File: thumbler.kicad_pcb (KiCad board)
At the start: 2 copper layers, 128 parts, among them J1 Conn_01x07, J2 Conn_01x05, J3 Conn_01x07, J4 Conn_01x05

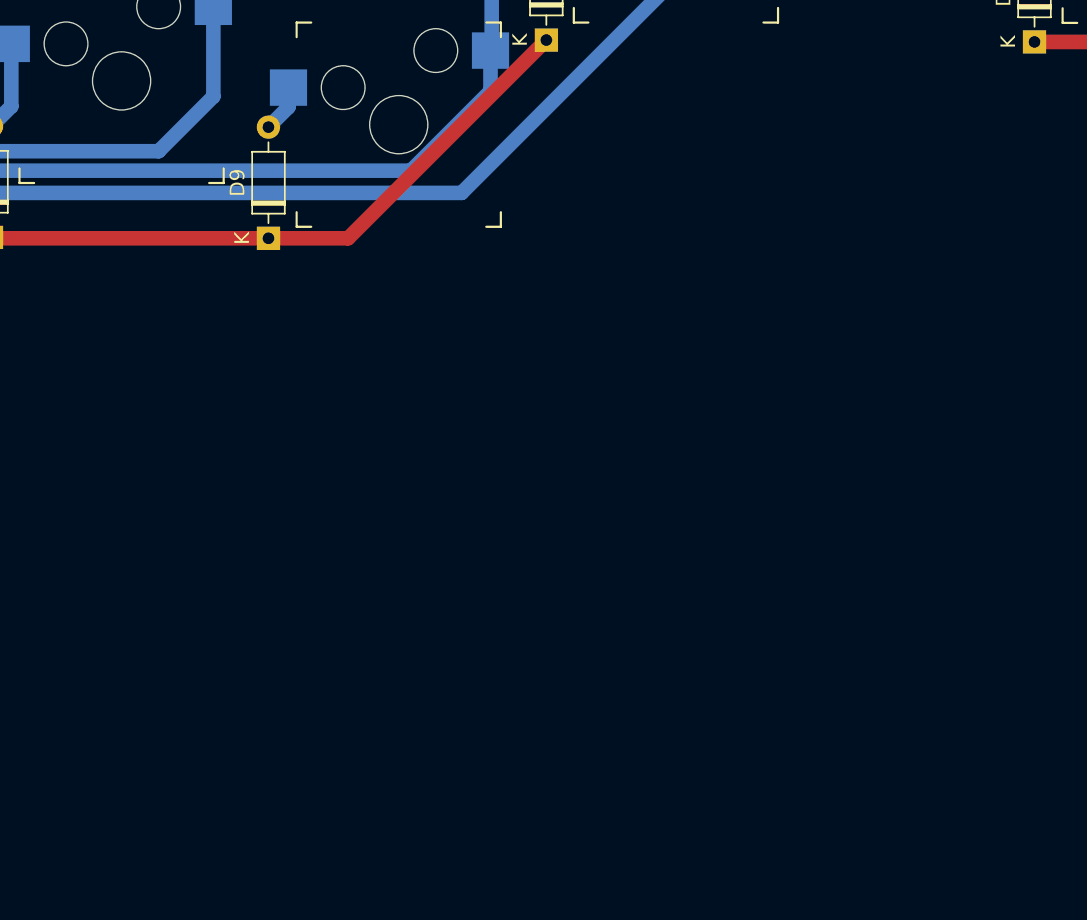
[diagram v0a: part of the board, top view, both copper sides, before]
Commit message: add footprint for ANO
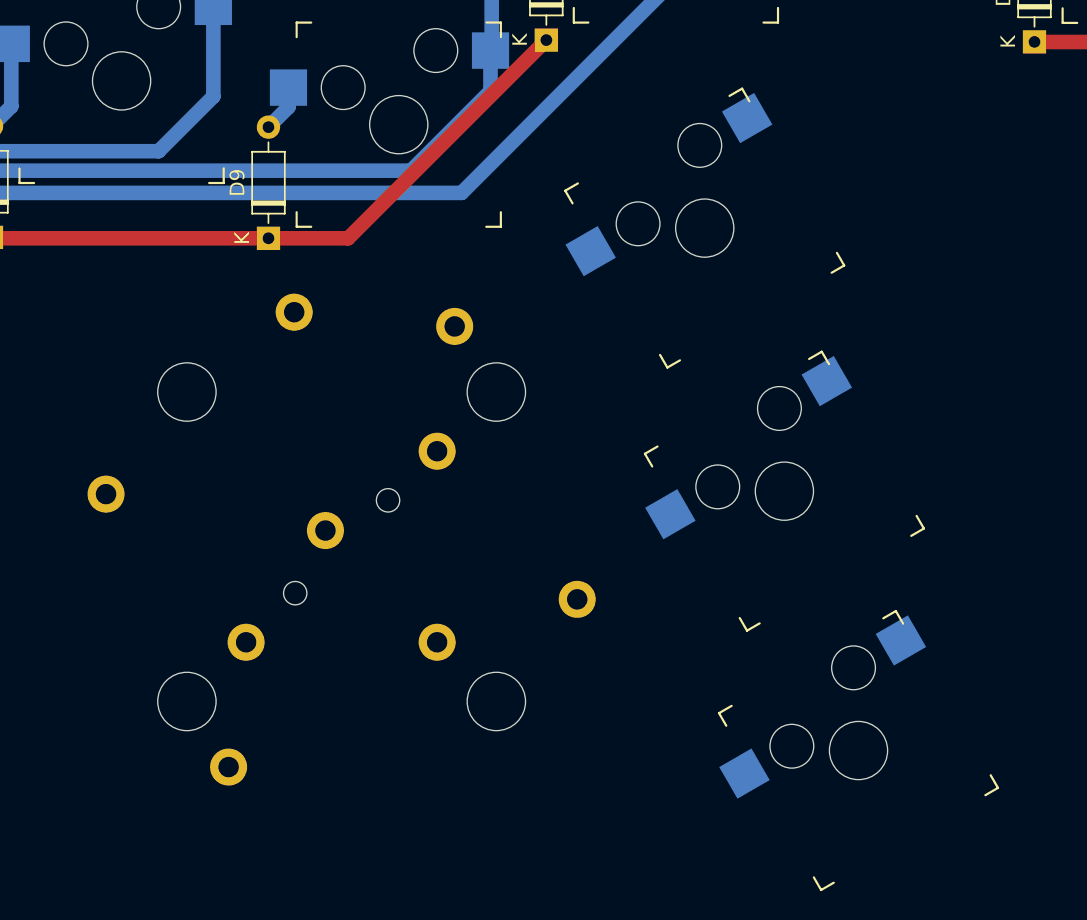
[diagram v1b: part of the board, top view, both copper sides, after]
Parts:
- added S9: Kailh_Hotplug, keyswitches:Kailh_socket_MX_platemount, F.Cu at (290.6, 222.8)
- added S9: Kailh_Hotplug, keyswitches:Kailh_socket_MX_platemount, F.Cu at (285.5, 205.0)
- added S9: Kailh_Hotplug, keyswitches:Kailh_socket_MX_platemount, F.Cu at (280.0, 187.0)
- added X1: ENCODER_ANO, ENCODER_ANO, B.Cu at (255.1, 208.8)

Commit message: more protection, more footprints
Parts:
- removed J3: Conn_01x07, Connector_PinHeader_2.54mm:PinHeader_1x07_P2.54mm_Vertical
- removed the S9 at (290.6, 222.8)
- removed the S9 at (285.5, 205.0)
- removed the S9 at (280.0, 187.0)
- added C1: 1u, Capacitor_SMD:C_0805_2012Metric_Pad1.18x1.45mm_HandSolder, F.Cu at (341.6, 301.8)
- added C10: 10n, Capacitor_SMD:C_0805_2012Metric_Pad1.18x1.45mm_HandSolder, F.Cu at (200.1, 314.3)
- added C11: Cext, Capacitor_SMD:C_0805_2012Metric_Pad1.18x1.45mm_HandSolder, F.Cu at (341.6, 298.8)
- added C12: Cext, Capacitor_SMD:C_0805_2012Metric_Pad1.18x1.45mm_HandSolder, F.Cu at (331.7, 307.5)
- added C13: 1u, Capacitor_SMD:C_0805_2012Metric_Pad1.18x1.45mm_HandSolder, F.Cu at (356.5, 282.2)
- added C14: 1u, Capacitor_SMD:C_0805_2012Metric_Pad1.18x1.45mm_HandSolder, F.Cu at (331.7, 310.5)
- added C15: 4u7, Capacitor_SMD:C_0805_2012Metric_Pad1.18x1.45mm_HandSolder, F.Cu at (214.4, 319.8)
- added C16: 4u7, Capacitor_SMD:C_0805_2012Metric_Pad1.18x1.45mm_HandSolder, F.Cu at (318.5, 321.0)
- added C17: 100n, Capacitor_SMD:C_0805_2012Metric_Pad1.18x1.45mm_HandSolder, F.Cu at (312.5, 328.2)
- added C18: 100n, Capacitor_SMD:C_0805_2012Metric_Pad1.18x1.45mm_HandSolder, F.Cu at (304.1, 339.5)
- added C19: 100n, Capacitor_SMD:C_0805_2012Metric_Pad1.18x1.45mm_HandSolder, F.Cu at (361.3, 282.2)
- added C2: 1u, Capacitor_SMD:C_0805_2012Metric_Pad1.18x1.45mm_HandSolder, F.Cu at (204.9, 314.3)
- added C20: 1u, Capacitor_SMD:C_0805_2012Metric_Pad1.18x1.45mm_HandSolder, F.Cu at (336.2, 304.1)
- added C21: 10n, Capacitor_SMD:C_0805_2012Metric_Pad1.18x1.45mm_HandSolder, F.Cu at (306.5, 335.3)
- added C22: 100n, Capacitor_SMD:C_0805_2012Metric_Pad1.18x1.45mm_HandSolder, F.Cu at (356.5, 285.2)
- added C3: 4u7, Capacitor_SMD:C_0805_2012Metric_Pad1.18x1.45mm_HandSolder, F.Cu at (209.7, 314.3)
- added C4: 4u7, Capacitor_SMD:C_0805_2012Metric_Pad1.18x1.45mm_HandSolder, F.Cu at (214.5, 314.3)
- added C5: 100n, Capacitor_SMD:C_0805_2012Metric_Pad1.18x1.45mm_HandSolder, F.Cu at (214.2, 330.7)
- added C6: 100n, Capacitor_SMD:C_0805_2012Metric_Pad1.18x1.45mm_HandSolder, F.Cu at (214.5, 325.3)
- added C7: 100n, Capacitor_SMD:C_0805_2012Metric_Pad1.18x1.45mm_HandSolder, F.Cu at (306.5, 332.3)
- added C8: 1u, Capacitor_SMD:C_0805_2012Metric_Pad1.18x1.45mm_HandSolder, F.Cu at (324.5, 316.9)
- added C9: 100n, Capacitor_SMD:C_0805_2012Metric_Pad1.18x1.45mm_HandSolder, F.Cu at (349.3, 290.3)
- added D63: RED, LED_SMD:LED_1206_3216Metric_Pad1.42x1.75mm_HandSolder, F.Cu at (190.1, 81.6)
- added D64: 1N4148, Diode_THT:D_DO-35_SOD27_P7.62mm_Horizontal, F.Cu at (272.2, 199.0)
- added D65: 1N4148, Diode_THT:D_DO-35_SOD27_P7.62mm_Horizontal, F.Cu at (270.6, 220.5)
- added D66: 1N4148, Diode_THT:D_DO-35_SOD27_P7.62mm_Horizontal, F.Cu at (269.4, 240.7)
- added D67: RED, LED_SMD:LED_1206_3216Metric_Pad1.42x1.75mm_HandSolder, F.Cu at (307.1, 329.1)
- added D68: WHITE, LED_SMD:LED_1206_3216Metric_Pad1.42x1.75mm_HandSolder, F.Cu at (467.2, 77.7)
- added D69: 1N4148, Diode_THT:D_DO-35_SOD27_P7.62mm_Horizontal, F.Cu at (343.2, 198.0)
- added D70: 1N4148, Diode_THT:D_DO-35_SOD27_P7.62mm_Horizontal, F.Cu at (347.3, 217.8)
- added D71: 1N4148, Diode_THT:D_DO-35_SOD27_P7.62mm_Horizontal, F.Cu at (353.1, 236.5)
- added D72: WHITE, LED_SMD:LED_1206_3216Metric_Pad1.42x1.75mm_HandSolder, F.Cu at (467.2, 82.5)
- added D73: WHITE, LED_SMD:LED_1206_3216Metric_Pad1.42x1.75mm_HandSolder, F.Cu at (467.2, 72.9)
- added D74: B5819W, Diode_SMD:D_SOD-123, F.Cu at (196.7, 63.8)
- added D75: B5819W, Diode_SMD:D_SOD-123, F.Cu at (409.4, 62.6)
- added F1: 350mA, Resistor_SMD:R_1812_4532Metric_Pad1.30x3.40mm_HandSolder, F.Cu at (184.7, 63.7)
- added F2: 350mA, Resistor_SMD:R_1812_4532Metric_Pad1.30x3.40mm_HandSolder, F.Cu at (399.4, 62.4)
- added FB1: 90R @ 100MHz, Inductor_SMD:L_0805_2012Metric_Pad1.15x1.40mm_HandSolder, F.Cu at (318.5, 324.0)
- added FB2: 90R @ 100MHz, Inductor_SMD:L_0805_2012Metric_Pad1.15x1.40mm_HandSolder, F.Cu at (420.3, 62.7)
- added J6: Conn_01x04, Connector_PinHeader_2.54mm:PinHeader_2x02_P2.54mm_Vertical, F.Cu at (149.4, 199.6)
- added J7: DIN-5_180degree, Connector_DIN:DIN5_180_CP-2350, F.Cu at (362.9, 79.9)
- added J8: Conn_01x04, Connector_PinHeader_2.54mm:PinHeader_2x02_P2.54mm_Vertical, F.Cu at (497.6, 194.4)
- added JP1: SolderJumper_2_Open, Jumper:SolderJumper-2_P1.3mm_Open_TrianglePad1.0x1.5mm, F.Cu at (261.3, 68.0)
- added R1: 470R, Resistor_SMD:R_0805_2012Metric_Pad1.20x1.40mm_HandSolder, F.Cu at (323.3, 321.0)
- added R10: 470R, Resistor_SMD:R_0805_2012Metric_Pad1.20x1.40mm_HandSolder, F.Cu at (323.3, 323.9)
- added R11: 470R, Resistor_SMD:R_0805_2012Metric_Pad1.20x1.40mm_HandSolder, F.Cu at (316.1, 331.2)
- added R12: 470R, Resistor_SMD:R_0805_2012Metric_Pad1.20x1.40mm_HandSolder, F.Cu at (328.0, 319.9)
- added R13: 470R, Resistor_SMD:R_0805_2012Metric_Pad1.20x1.40mm_HandSolder, F.Cu at (346.3, 302.1)
- added R14: 470R, Resistor_SMD:R_0805_2012Metric_Pad1.20x1.40mm_HandSolder, F.Cu at (352.4, 296.2)
- added R15: 470R, Resistor_SMD:R_0805_2012Metric_Pad1.20x1.40mm_HandSolder, F.Cu at (334.0, 316.4)
- added R16: 10K, Resistor_SMD:R_0805_2012Metric_Pad1.20x1.40mm_HandSolder, F.Cu at (328.0, 322.8)
- added R17: 470R, Resistor_SMD:R_0805_2012Metric_Pad1.20x1.40mm_HandSolder, F.Cu at (316.1, 334.1)
- added R18: 470R, Resistor_SMD:R_0805_2012Metric_Pad1.20x1.40mm_HandSolder, F.Cu at (323.2, 326.9)
- added R19: 470R, Resistor_SMD:R_0805_2012Metric_Pad1.20x1.40mm_HandSolder, F.Cu at (347.7, 293.2)
- added R2: 10K, Resistor_SMD:R_0805_2012Metric_Pad1.20x1.40mm_HandSolder, F.Cu at (347.7, 296.2)
- added R20: 1K, Resistor_SMD:R_0805_2012Metric_Pad1.20x1.40mm_HandSolder, F.Cu at (341.2, 307.7)
- added R21: 1K, Resistor_SMD:R_0805_2012Metric_Pad1.20x1.40mm_HandSolder, F.Cu at (336.5, 310.0)
- added R22: 470R, Resistor_SMD:R_0805_2012Metric_Pad1.20x1.40mm_HandSolder, F.Cu at (331.7, 313.4)
- added R23: 1K, Resistor_SMD:R_0805_2012Metric_Pad1.20x1.40mm_HandSolder, F.Cu at (355.3, 288.2)
- added R24: 470R, Resistor_SMD:R_0805_2012Metric_Pad1.20x1.40mm_HandSolder, B.Cu at (438.8, 184.6)
- added R25: 10K, Resistor_SMD:R_0805_2012Metric_Pad1.20x1.40mm_HandSolder, F.Cu at (352.4, 293.2)
- added R26: 470R, Resistor_SMD:R_0805_2012Metric_Pad1.20x1.40mm_HandSolder, F.Cu at (318.5, 326.9)
- added R27: 470R, Resistor_SMD:R_0805_2012Metric_Pad1.20x1.40mm_HandSolder, F.Cu at (329.3, 316.8)
- added R28: 470R, Resistor_SMD:R_0805_2012Metric_Pad1.20x1.40mm_HandSolder, F.Cu at (336.5, 307.1)
- added R3: 22R, Resistor_SMD:R_0805_2012Metric_Pad1.20x1.40mm_HandSolder, F.Cu at (346.3, 299.1)
- added R4: 1K, Resistor_SMD:R_0805_2012Metric_Pad1.20x1.40mm_HandSolder, F.Cu at (311.3, 335.2)
- added R5: 22R, Resistor_SMD:R_0805_2012Metric_Pad1.20x1.40mm_HandSolder, F.Cu at (172.7, 74.7)
- added R6: 22R, Resistor_SMD:R_0805_2012Metric_Pad1.20x1.40mm_HandSolder, F.Cu at (341.2, 304.8)
- added R7: 22R, Resistor_SMD:R_0805_2012Metric_Pad1.20x1.40mm_HandSolder, F.Cu at (361.3, 285.1)
- added R8: 1K, Resistor_SMD:R_0805_2012Metric_Pad1.20x1.40mm_HandSolder, F.Cu at (308.9, 338.2)
- added R9: 470R, Resistor_SMD:R_0805_2012Metric_Pad1.20x1.40mm_HandSolder, B.Cu at (189.3, 187.9)
- added S63: Kailh_Hotplug, keyswitches:Kailh_socket_MX_platemount, F.Cu at (281.2, 190.9)
- added S64: Kailh_Hotplug, keyswitches:Kailh_socket_MX_platemount, F.Cu at (279.5, 212.2)
- added S65: Kailh_Hotplug, keyswitches:Kailh_socket_MX_platemount, F.Cu at (278.3, 232.5)
- added S66: RKJXV122400R, Alps:RKJXV122400R, F.Cu at (382.8, 206.4)
- added S67: Kailh_Hotplug, keyswitches:Kailh_socket_MX_platemount, F.Cu at (352.2, 189.8)
- added S68: Kailh_Hotplug, keyswitches:Kailh_socket_MX_platemount, F.Cu at (356.2, 209.7)
- added S69: Kailh_Hotplug, keyswitches:Kailh_socket_MX_platemount, F.Cu at (361.9, 228.4)
- added SW1: SW_Push, Button_Switch_THT:SW_PUSH-12mm, B.Cu at (160.2, 199.2)
- added SW2: SW_DIP_x05, Button_Switch_THT:SW_DIP_SPSTx05_Slide_9.78x14.88mm_W7.62mm_P2.54mm, B.Cu at (161.2, 205.6)
- added SW3: SW_Push, Button_Switch_THT:SW_PUSH-12mm, B.Cu at (464.6, 200.1)
- added SW4: SW_DIP_x05, Button_Switch_THT:SW_DIP_SPSTx05_Slide_9.78x14.88mm_W7.62mm_P2.54mm, B.Cu at (465.8, 207.3)
- added TP1: TestPoint, TestPoint:TestPoint_Pad_D2.0mm, F.Cu at (161.5, 251.5)
- added TP10: TestPoint, TestPoint:TestPoint_Pad_D2.0mm, F.Cu at (155.9, 234.4)
- added TP11: TestPoint, TestPoint:TestPoint_Pad_D2.0mm, F.Cu at (149.8, 238.4)
- added TP12: TestPoint, TestPoint:TestPoint_Pad_D2.0mm, F.Cu at (149.0, 250.6)
- added TP13: TestPoint, TestPoint:TestPoint_Pad_D2.0mm, F.Cu at (145.8, 238.3)
- added TP14: TestPoint, TestPoint:TestPoint_Pad_D2.0mm, F.Cu at (158.4, 263.6)
- added TP15: TestPoint, TestPoint:TestPoint_Pad_D2.0mm, F.Cu at (153.1, 250.1)
- added TP16: TestPoint, TestPoint:TestPoint_Pad_D2.0mm, F.Cu at (159.1, 245.5)
- added TP17: TestPoint, TestPoint:TestPoint_Pad_D2.0mm, F.Cu at (165.6, 255.4)
- added TP18: TestPoint, TestPoint:TestPoint_Pad_D2.0mm, F.Cu at (153.9, 238.4)
- added TP19: TestPoint, TestPoint:TestPoint_Pad_D2.0mm, F.Cu at (148.7, 242.5)
- added TP2: TestPoint, TestPoint:TestPoint_Pad_D2.0mm, F.Cu at (155.0, 245.5)
- added TP20: TestPoint, TestPoint:TestPoint_Pad_D2.0mm, F.Cu at (169.6, 251.4)
- added TP21: TestPoint, TestPoint:TestPoint_Pad_D2.0mm, F.Cu at (422.8, 270.0)
- added TP22: TestPoint, TestPoint:TestPoint_Pad_D2.0mm, F.Cu at (422.6, 284.1)
- added TP23: TestPoint, TestPoint:TestPoint_Pad_D2.0mm, F.Cu at (429.0, 252.6)
- added TP24: TestPoint, TestPoint:TestPoint_Pad_D2.0mm, F.Cu at (422.8, 277.2)
- added TP25: TestPoint, TestPoint:TestPoint_Pad_D2.0mm, F.Cu at (433.1, 252.1)
- added TP26: TestPoint, TestPoint:TestPoint_Pad_D2.0mm, F.Cu at (421.2, 263.3)
- added TP27: TestPoint, TestPoint:TestPoint_Pad_D2.0mm, F.Cu at (419.5, 257.1)
- added TP28: TestPoint, TestPoint:TestPoint_Pad_D2.0mm, F.Cu at (428.9, 263.1)
- added TP29: TestPoint, TestPoint:TestPoint_Pad_D2.0mm, F.Cu at (430.9, 271.0)
- added TP3: TestPoint, TestPoint:TestPoint_Pad_D2.0mm, F.Cu at (151.9, 230.3)
- added TP30: TestPoint, TestPoint:TestPoint_Pad_D2.0mm, F.Cu at (429.2, 256.6)
- added TP31: TestPoint, TestPoint:TestPoint_Pad_D2.0mm, F.Cu at (431.7, 277.8)
- added TP32: TestPoint, TestPoint:TestPoint_Pad_D2.0mm, F.Cu at (432.4, 284.3)
- added TP33: TestPoint, TestPoint:TestPoint_Pad_D2.0mm, F.Cu at (414.5, 284.3)
- added TP34: TestPoint, TestPoint:TestPoint_Pad_D2.0mm, F.Cu at (416.1, 271.5)
- added TP35: TestPoint, TestPoint:TestPoint_Pad_D2.0mm, F.Cu at (438.2, 263.4)
- added TP36: TestPoint, TestPoint:TestPoint_Pad_D2.0mm, F.Cu at (421.2, 249.6)
- added TP4: TestPoint, TestPoint:TestPoint_Pad_D2.0mm, F.Cu at (161.5, 255.5)
- added TP5: TestPoint, TestPoint:TestPoint_Pad_D2.0mm, F.Cu at (144.7, 244.2)
- added TP6: TestPoint, TestPoint:TestPoint_Pad_D2.0mm, F.Cu at (162.2, 239.9)
- added TP7: TestPoint, TestPoint:TestPoint_Pad_D2.0mm, F.Cu at (168.7, 247.3)
- added TP8: TestPoint, TestPoint:TestPoint_Pad_D2.0mm, F.Cu at (154.4, 263.7)
- added TP9: TestPoint, TestPoint:TestPoint_Pad_D2.0mm, F.Cu at (158.4, 259.6)
- added U1: MCP1700-3302E_SOT89, Package_TO_SOT_SMD:SOT-89-3, F.Cu at (193.8, 74.3)
- added U2: STM32F072C8Tx, Package_QFP:LQFP-48_7x7mm_P0.5mm, F.Cu at (207.4, 203.0)
- added U3: MCP1700-3302E_SOT89, Package_TO_SOT_SMD:SOT-89-3, F.Cu at (451.7, 71.0)
- added U4: STM32F072C8Tx, Package_QFP:LQFP-48_7x7mm_P0.5mm, F.Cu at (440.1, 200.6)
- J1: value Conn_01x07 -> Conn_01x04; footprint Connector_PinHeader_2.54mm:PinHeader_1x07_P2.54mm_Vertical -> Connector_PinHeader_2.54mm:PinHeader_2x02_P2.54mm_Vertical
- J2: value Conn_01x05 -> DIN-5_180degree; footprint Connector_PinHeader_2.54mm:PinHeader_1x05_P2.54mm_Vertical -> Connector_DIN:DIN5_180_CP-2350
- J4: value Conn_01x05 -> Conn_01x04; footprint Connector_PinHeader_2.54mm:PinHeader_1x05_P2.54mm_Vertical -> Connector_PinHeader_2.54mm:PinHeader_2x02_P2.54mm_Vertical
- X1: footprint ENCODER_ANO -> Rotary_Encoder:ENCODER_ANO; moved to F.Cu
- moved J2 143.2 mm to (284.4, 79.3), turned to 90 degrees
- moved J4 90.0 mm to (497.7, 203.1)
- moved J1 80.1 mm to (149.5, 209.2), turned to 90 degrees
- moved D32 64.0 mm to (480.6, 128.6)
- moved D33 64.0 mm to (480.6, 185.5)
- moved D34 64.0 mm to (471.2, 147.9)
- moved D35 64.0 mm to (471.2, 166.5)
- moved D36 64.0 mm to (461.6, 109.7)
- moved D37 64.0 mm to (461.6, 128.7)
- moved D38 64.0 mm to (461.6, 185.5)
- moved D39 64.0 mm to (442.7, 105.5)
- moved D40 64.0 mm to (442.7, 124.6)
- moved D41 64.0 mm to (442.7, 143.5)
- moved D42 64.0 mm to (442.7, 162.6)
- moved D43 64.0 mm to (442.7, 181.7)
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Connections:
- net Col1R renamed Net-(R17-Pad2)
- net Col2R renamed Net-(R18-Pad2)
- net Col3R renamed Net-(R22-Pad2)
- net Col4R renamed Net-(R24-Pad2)
- net Col5R renamed Net-(R26-Pad2)
- net Col6R renamed Net-(R27-Pad2)
- net Col7R renamed Net-(R28-Pad2)
- D1 pad 1: Row2L -> L_ROW2
- D10 pad 1: Row1L -> L_ROW1
- D11 pad 1: Row2L -> L_ROW2
- D12 pad 1: Row3L -> L_ROW3
- D13 pad 1: Row4L -> L_ROW4
- D14 pad 1: Row5L -> L_ROW5
- D15 pad 1: Row1L -> L_ROW1
- D16 pad 1: Row2L -> L_ROW2
- D17 pad 1: Row3L -> L_ROW3
- D18 pad 1: Row4L -> L_ROW4
- D19 pad 1: Row5L -> L_ROW5
- D2 pad 1: Row3L -> L_ROW3
- D20 pad 1: Row1L -> L_ROW1
- D21 pad 1: Row2L -> L_ROW2
- D22 pad 1: Row3L -> L_ROW3
- D23 pad 1: Row4L -> L_ROW4
- D24 pad 1: Row5L -> L_ROW5
- D25 pad 1: Row1L -> L_ROW1
- D26 pad 1: Row2L -> L_ROW2
- D27 pad 1: Row5L -> L_ROW5
- D28 pad 1: Row3L -> L_ROW3
- D29 pad 1: Row4L -> L_ROW4
- D3 pad 1: Row4L -> L_ROW4
- D30 pad 1: Row2L -> L_ROW2
- D31 pad 1: Row5L -> L_ROW5
- D32 pad 1: Row2R -> R_ROW2
- D33 pad 1: Row5R -> R_ROW5
- D34 pad 1: Row3R -> R_ROW3
- D35 pad 1: Row4R -> R_ROW4
- D36 pad 1: Row1R -> R_ROW1
- D37 pad 1: Row2R -> R_ROW2
- D38 pad 1: Row5R -> R_ROW5
- D39 pad 1: Row1R -> R_ROW1
- D4 pad 1: Row5L -> L_ROW5
- D40 pad 1: Row2R -> R_ROW2
- D41 pad 1: Row3R -> R_ROW3
- D42 pad 1: Row4R -> R_ROW4
- D43 pad 1: Row5R -> R_ROW5
- D44 pad 1: Row1R -> R_ROW1
- D45 pad 1: Row2R -> R_ROW2
- D46 pad 1: Row3R -> R_ROW3
- D47 pad 1: Row4R -> R_ROW4
- D48 pad 1: Row5R -> R_ROW5
- D49 pad 1: Row1R -> R_ROW1
- D5 pad 1: Row1L -> L_ROW1
- D50 pad 1: Row2R -> R_ROW2
- D51 pad 1: Row3R -> R_ROW3
- D52 pad 1: Row4R -> R_ROW4
- D53 pad 1: Row5R -> R_ROW5
- D54 pad 1: Row1R -> R_ROW1
- D55 pad 1: Row2R -> R_ROW2
- D56 pad 1: Row3R -> R_ROW3
- D57 pad 1: Row4R -> R_ROW4
- D58 pad 1: Row5R -> R_ROW5
- D59 pad 1: Row2R -> R_ROW2
- D6 pad 1: Row2L -> L_ROW2
- D60 pad 1: Row3R -> R_ROW3
- D61 pad 1: Row4R -> R_ROW4
- D62 pad 1: Row5R -> R_ROW5
- D7 pad 1: Row3L -> L_ROW3
- D8 pad 1: Row4L -> L_ROW4
- D9 pad 1: Row5L -> L_ROW5
- J1 pad 1: Col1L -> +3V3
- J1 pad 2: Col2L -> L_RX
- J1 pad 3: Col3L -> L_TX
- J1 pad 4: Col4L -> GND
- J2 pad 1: Row1L -> GND
- J2 pad 2: Row2L -> Net-(J2-Pad2)
- J2 pad 3: Row3L -> L_RX
- J2 pad 4: Row4L -> +5V
- J2 pad 5: Row5L -> L_TX
- J4 pad 1: Row1R -> +3V3
- J4 pad 2: Row2R -> R_RX
- J4 pad 3: Row3R -> R_TX
- J4 pad 4: Row4R -> GND
- S1 pad 2: Col1L -> Net-(R15-Pad2)
- S10 pad 2: Col3L -> Net-(R12-Pad2)
- S11 pad 2: Col3L -> Net-(R12-Pad2)
- S12 pad 2: Col3L -> Net-(R12-Pad2)
- S13 pad 2: Col3L -> Net-(R12-Pad2)
- S14 pad 2: Col3L -> Net-(R12-Pad2)
- S15 pad 2: Col4L -> Net-(R11-Pad2)
- S16 pad 2: Col4L -> Net-(R11-Pad2)
- S17 pad 2: Col4L -> Net-(R11-Pad2)
- S18 pad 2: Col4L -> Net-(R11-Pad2)
- S19 pad 2: Col4L -> Net-(R11-Pad2)
- S2 pad 2: Col1L -> Net-(R15-Pad2)
- S20 pad 2: Col5L -> Net-(R10-Pad2)
- S21 pad 2: Col5L -> Net-(R10-Pad2)
- S22 pad 2: Col5L -> Net-(R10-Pad2)
- S23 pad 2: Col5L -> Net-(R10-Pad2)
- S24 pad 2: Col5L -> Net-(R10-Pad2)
- S25 pad 2: Col6L -> Net-(R9-Pad2)
- S26 pad 2: Col6L -> Net-(R9-Pad2)
- S27 pad 2: Col6L -> Net-(R9-Pad2)
- S28 pad 2: Col7L -> Net-(R1-Pad2)
- S29 pad 2: Col7L -> Net-(R1-Pad2)
- S3 pad 2: Col1L -> Net-(R15-Pad2)
- S30 pad 2: Col7L -> Net-(R1-Pad2)
- S31 pad 2: Col7L -> Net-(R1-Pad2)
- S4 pad 2: Col1L -> Net-(R15-Pad2)
- S5 pad 2: Col2L -> Net-(R13-Pad2)
- S6 pad 2: Col2L -> Net-(R13-Pad2)
- S7 pad 2: Col2L -> Net-(R13-Pad2)
- S8 pad 2: Col2L -> Net-(R13-Pad2)
- S9 pad 2: Col2L -> Net-(R13-Pad2)
- X1 pad A: (no net) -> L_ENC_A
- X1 pad B: (no net) -> L_ENC_B
- X1 pad COM_A: (no net) -> GND
- X1 pad COM_B: (no net) -> GND
- X1 pad S1: (no net) -> L_ENC_BN
- X1 pad S2: (no net) -> L_ENC_DN
- X1 pad S3: (no net) -> L_ENC_RT
- X1 pad S4: (no net) -> L_ENC_UP
- X1 pad S5: (no net) -> L_ENC_LF
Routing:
- net Row5R: track 171.5 -> 0.00 mm
- net Row5L: track 161.9 -> 0.00 mm
- net Row4R: track 150.4 -> 0.00 mm
- net Row2R: track 148.0 -> 0.00 mm
- net Row1R: track 145.1 -> 0.00 mm
- net Row2L: track 145.0 -> 0.00 mm
- net Row3R: track 143.8 -> 0.00 mm
- net Row4L: track 140.4 -> 0.00 mm
- net Row1L: track 131.6 -> 0.00 mm
- net L_ROW2: track 0.00 -> 128.4 mm
- net Col1L: track 127.3 -> 0.00 mm
- net Row3L: track 126.0 -> 0.00 mm
- net Col2L: track 125.5 -> 0.00 mm
- net L_ROW5: track 0.00 -> 124.5 mm
- net R_ROW2: track 0.00 -> 124.5 mm
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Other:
- net class Default: clearance 0.2 -> 0.127
- net class Power added: clearance 0.3, trace_width 0.35, via_dia 0.8, via_drill 0.4
- rule trace_clearance: 0.2 -> 0.127
- rule trace_min: 0.2 -> 0.128
- rule via_min_drill: 0.3 -> 0.2

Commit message: footprints done
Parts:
- removed R16: 10K, Resistor_SMD:R_0805_2012Metric_Pad1.20x1.40mm_HandSolder
- added J3: USB_B_Micro, Connector_USB:USB_Micro-B_HRO_U-F-M5SS-W-1, F.Cu at (491.8, 72.2)
- added J5: USB_B_Micro, Connector_USB:USB_Micro-B_HRO_U-F-M5SS-W-1, F.Cu at (166.0, 73.3)
- added TP37: TestPoint, TestPoint:TestPoint_Pad_D2.0mm, F.Cu at (197.4, 73.1)
- added TP38: TestPoint, TestPoint:TestPoint_Pad_D2.0mm, F.Cu at (477.5, 63.8)
- R1, R10, R11, R12, R13, R14, R15, R17, R18, R19, R22, R26, R27, R28, TP1, TP10, TP11, TP12, TP13, TP14, TP15, TP16, TP17, TP18, TP19, TP2, TP20, TP21, TP22, TP23, TP24, TP25, TP26, TP27, TP28, TP29, TP3, TP30, TP31, TP32, TP33, TP34, TP35, TP36, TP4, TP5, TP6, TP7, TP8, TP9: moved to B.Cu
- moved R8 292.7 mm to (451.5, 82.7)
- moved D67 288.8 mm to (451.8, 79.1)
- moved R4 288.7 mm to (190.0, 73.2), turned to 90 degrees
- moved FB1 285.7 mm to (181.6, 73.2), turned to 90 degrees
- moved R3 284.5 mm to (164.6, 80.3), turned to 90 degrees
- moved C1 276.5 mm to (186.0, 73.2), turned to 90 degrees
- moved R6 270.8 mm to (490.4, 78.8), turned to 90 degrees
- moved C14 265.6 mm to (444.7, 70.1)
- moved R21 262.5 mm to (465.1, 81.2), turned to 270 degrees
- moved R20 260.6 mm to (470.0, 81.2), turned to 270 degrees
- moved R7 245.2 mm to (493.7, 78.8), turned to 270 degrees
- moved R23 239.0 mm to (474.8, 81.2), turned to 270 degrees
- moved C15 238.4 mm to (432.0, 222.3)
- moved C13 236.2 mm to (451.3, 65.8)
- moved C2 230.4 mm to (187.6, 84.5)
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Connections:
- D74 pad 1: Net-(D74-Pad1) -> +5V
- D75 pad 1: Net-(D75-Pad1) -> +5V
- F1 pad 1: +5V -> Net-(F1-Pad1)
- F2 pad 1: Net-(D75-Pad2) -> Net-(F2-Pad1)
- F2 pad 2: +5V -> Net-(D75-Pad2)
- FB1 pad 2: Net-(D74-Pad1) -> +5V
- FB2 pad 2: Net-(D75-Pad1) -> +5V
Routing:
- net Net-(R24-Pad2): track 91.2 -> 76.0 mm
- net Net-(R9-Pad2): track 91.1 -> 76.1 mm
- net Net-(D69-Pad2): track 0.00 -> 3.63 mm
- net Net-(D66-Pad2): track 0.00 -> 3.54 mm
- net Net-(D70-Pad2): track 0.00 -> 3.54 mm
- net Net-(D71-Pad2): track 0.00 -> 3.54 mm
- net Net-(D65-Pad2): track 0.00 -> 3.50 mm
- net Net-(D64-Pad2): track 0.00 -> 3.50 mm

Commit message: layout wip
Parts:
- C10, C15, C16, C17, C18, C19, C20, C21, C3, C4, C5, C6, C7, C8: footprint Capacitor_SMD:C_0805_2012Metric_Pad1.18x1.45mm_HandSolder -> Capacitor_SMD:C_0603_1608Metric_Pad1.08x0.95mm_HandSolder; moved to B.Cu
- C9, D63, D67, J2, J7, JP1, R4, R8: moved to B.Cu
- moved C18 191.6 mm to (413.6, 144.5)
- moved C16 175.3 mm to (413.6, 143.0)
- moved C21 174.6 mm to (401.3, 149.6), turned to 180 degrees
- moved C17 161.1 mm to (413.0, 152.9)
- moved C8 152.6 mm to (200.6, 154.2), turned to 180 degrees
- moved C7 147.3 mm to (202.6, 146.8), turned to 180 degrees
- moved C19 145.4 mm to (403.3, 143.9), turned to 180 degrees
- moved C9 127.4 mm to (275.1, 149.6), turned to 270 degrees
- moved J4 126.0 mm to (377.1, 153.4)
- moved R25 126.0 mm to (366.6, 169.3)
- moved SW3 126.0 mm to (355.3, 149.7)
- moved SW4 126.0 mm to (356.4, 156.9)
- moved J8 126.0 mm to (377.0, 144.7)
- moved C22 121.2 mm to (346.6, 148.7)
- moved J7 114.3 mm to (326.3, 187.5), turned to 90 degrees
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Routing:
- net +3V3: track 0.00 -> 22.2 mm, vias 0 -> 8
- net R_PTR_X: track 0.00 -> 3.89 mm
- net R_PTR_Y: track 0.00 -> 3.68 mm
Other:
- rule via_min_drill: 0.2 -> 0.3
- rule via_min_size: 0.4 -> 0.6

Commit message: left side re-layout mostly done
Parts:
- removed the D1 at (255.3, 189.3)
- removed the D2 at (255.3, 208.3)
- removed the D3 at (255.3, 227.2)
- removed the D30 at (141.3, 200.1)
- removed the D31 at (141.3, 257.1)
- removed the D6 at (236.3, 203.2)
- removed the S1 at (264.2, 181.0)
- removed the S27 at (169.2, 249.0)
- removed the S28 at (159.7, 211.0)
- removed the S4 at (264.2, 238.0)
- added D25: 1N4148, Diode_THT:D_DO-35_SOD27_P7.62mm_Horizontal, F.Cu at (183.9, 197.1)
- added D32: 1N4148, Diode_THT:D_DO-35_SOD27_P7.62mm_Horizontal, F.Cu at (203.0, 182.0)
- added D33: 1N4148, Diode_THT:D_DO-35_SOD27_P7.62mm_Horizontal, F.Cu at (203.0, 201.1)
- added D34: 1N4148, Diode_THT:D_DO-35_SOD27_P7.62mm_Horizontal, F.Cu at (203.0, 220.1)
- added D35: 1N4148, Diode_THT:D_DO-35_SOD27_P7.62mm_Horizontal, F.Cu at (203.0, 239.2)
- added D73: 1N4148, Diode_THT:D_DO-35_SOD27_P7.62mm_Horizontal, F.Cu at (466.8, 219.6)
- added D74: 1N4148, Diode_THT:D_DO-35_SOD27_P7.62mm_Horizontal, F.Cu at (466.9, 238.5)
- added S25: Kailh_Hotplug, keyswitches:Kailh_socket_MX_platemount, F.Cu at (192.9, 227.2)
- added S32: Kailh_Hotplug, keyswitches:Kailh_socket_MX_platemount, F.Cu at (211.9, 212.1)
- added S33: Kailh_Hotplug, keyswitches:Kailh_socket_MX_platemount, F.Cu at (211.9, 231.2)
- added S68: Kailh_Hotplug, keyswitches:Kailh_socket_MX_platemount, F.Cu at (475.7, 211.4)
- added S69: Kailh_Hotplug, keyswitches:Kailh_socket_MX_platemount, F.Cu at (475.7, 230.4)
- moved TP23 212.0 mm to (562.2, 115.7)
- moved TP28 212.0 mm to (539.9, 96.5)
- moved TP38 212.0 mm to (539.9, 110.3)
- moved R15 212.0 mm to (495.1, 103.2)
- moved R20 212.0 mm to (503.1, 100.2)
- moved R24 212.0 mm to (514.7, 106.2)
- moved R26 212.0 mm to (516.8, 112.1)
- moved TP30 212.0 mm to (547.6, 96.7)
- moved TP37 212.0 mm to (557.0, 96.4)
- moved R13 212.0 mm to (495.2, 97.4)
- moved R16 212.0 mm to (516.9, 98.3)
- moved R19 212.0 mm to (494.7, 108.1)
- moved R25 212.0 mm to (522.2, 107.5)
- moved TP24 212.0 mm to (562.1, 101.6)
- moved TP25 212.0 mm to (547.8, 107.3)
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- renumbered C22 to C13, C13 to C14, C14 to C15, C15 to C16, C16 to C17, C17 to C18, C18 to C19, C19 to C20, C20 to C21, C21 to C22, C9 to C4, C4 to C5, C5 to C6, C6 to C7, C7 to C8, C8 to C9, D74 to D1, D63 to D2, D64 to D29, D29 to D3, D65 to D30, D66 to D31, D59 to D36, D60 to D37, D61 to D38, D62 to D39, D54 to D40, D55 to D41, D56 to D42, D57 to D43, D58 to D44, D68 to D45, D49 to D46, D50 to D47, D51 to D48, D52 to D49, D53 to D50, D72 to D51, D69 to D52, D70 to D53, D71 to D54, D73 to D55, D44 to D56, D45 to D57, D46 to D58, D47 to D59, D25 to D6, D48 to D60, D39 to D61, D40 to D62, D41 to D63, D42 to D64, D43 to D65, D75 to D66, D36 to D67, D37 to D68, D34 to D69, D35 to D70, D38 to D71, D32 to D72, D33 to D75, D67 to D76, J5 to J1, J1 to J2, J6 to J3, J2 to J4, J4 to J5, J7 to J6, J8 to J7, J3 to J8, R3 to R1, R13 to R10, R14 to R11, R15 to R12, R17 to R13, R20 to R14, R18 to R15, R19 to R16, R21 to R17, R23 to R18, R22 to R19, R5 to R2, R24 to R20, R6 to R21, R7 to R22, R25 to R23, R26 to R24, R27 to R25, R28 to R26, R8 to R27, R1 to R3, R9 to R5, R10 to R6, R2 to R7, R11 to R8, R12 to R9, S29 to S1, S63 to S27, S64 to S28, S65 to S29, S66 to S34, S59 to S35, S60 to S36, S61 to S37, S62 to S38, S54 to S39, S25 to S4, S55 to S40, S56 to S41, S57 to S42, S58 to S43, S67 to S44, S68 to S45, S69 to S46, S49 to S47, S50 to S48, S51 to S49, S52 to S50, S53 to S51, S44 to S52, S45 to S53, S46 to S54, S47 to S55, S48 to S56, S39 to S57, S40 to S58, S41 to S59, S42 to S60, S43 to S61, S36 to S62, S37 to S63, S34 to S64, S35 to S65, S38 to S66, S32 to S67, S33 to S70, TP37 to TP1, TP8 to TP10, TP9 to TP11, TP10 to TP12, TP11 to TP13, TP12 to TP14, TP14 to TP15, TP15 to TP16, TP16 to TP17, TP17 to TP18, TP18 to TP19, TP1 to TP2, TP19 to TP20, TP20 to TP21, TP38 to TP22, TP21 to TP23, TP22 to TP24, TP23 to TP25, TP24 to TP26, TP25 to TP27, TP26 to TP28, TP27 to TP29, TP2 to TP3, TP28 to TP30, TP29 to TP31, TP30 to TP32, TP31 to TP33, TP32 to TP34, TP33 to TP35, TP34 to TP36, TP35 to TP37, TP36 to TP38, TP3 to TP4, TP4 to TP5, TP5 to TP6, TP6 to TP7, TP7 to TP8, TP13 to TP9, U2 to U1, U1 to U2
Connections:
- D10 pad 2: Net-(D10-Pad2) -> Net-(D6-Pad2)
- D11 pad 1: L_ROW2 -> L_ROW1
- D11 pad 2: Net-(D11-Pad2) -> Net-(D6-Pad2)
- D12 pad 1: L_ROW3 -> L_ROW1
- D12 pad 2: Net-(D12-Pad2) -> Net-(D6-Pad2)
- D13 pad 1: L_ROW4 -> L_ROW1
- D13 pad 2: Net-(D13-Pad2) -> Net-(D6-Pad2)
- D14 pad 1: L_ROW5 -> L_ROW1
- D14 pad 2: Net-(D14-Pad2) -> Net-(D6-Pad2)
- D15 pad 2: Net-(D15-Pad2) -> Net-(D6-Pad2)
- D16 pad 1: L_ROW2 -> L_ROW1
- D16 pad 2: Net-(D16-Pad2) -> Net-(D6-Pad2)
- D17 pad 1: L_ROW3 -> L_ROW1
- D17 pad 2: Net-(D17-Pad2) -> Net-(D6-Pad2)
- D18 pad 1: L_ROW4 -> L_ROW1
- D18 pad 2: Net-(D18-Pad2) -> Net-(D6-Pad2)
- D19 pad 1: L_ROW5 -> L_ROW1
- D19 pad 2: Net-(D19-Pad2) -> Net-(D6-Pad2)
- D20 pad 2: Net-(D20-Pad2) -> Net-(D6-Pad2)
- D21 pad 1: L_ROW2 -> L_ROW1
- D21 pad 2: Net-(D21-Pad2) -> Net-(D6-Pad2)
- D22 pad 1: L_ROW3 -> L_ROW1
- D22 pad 2: Net-(D22-Pad2) -> Net-(D6-Pad2)
- D23 pad 1: L_ROW4 -> L_ROW1
- D23 pad 2: Net-(D23-Pad2) -> Net-(D6-Pad2)
- D24 pad 1: L_ROW5 -> L_ROW1
- D24 pad 2: Net-(D24-Pad2) -> Net-(D6-Pad2)
- D26 pad 1: L_ROW2 -> L_ROW1
- D26 pad 2: Net-(D26-Pad2) -> Net-(D6-Pad2)
- D27 pad 1: L_ROW5 -> L_ROW1
- D27 pad 2: Net-(D27-Pad2) -> Net-(D6-Pad2)
- D28 pad 1: L_ROW3 -> L_ROW1
- D28 pad 2: Net-(D28-Pad2) -> Net-(D6-Pad2)
- D4 pad 1: L_ROW5 -> L_ROW1
- D4 pad 2: Net-(D4-Pad2) -> Net-(D6-Pad2)
- D5 pad 2: Net-(D5-Pad2) (its old number) -> Net-(D6-Pad2)
- D6 pad 2: Net-(D25-Pad2) -> Net-(D6-Pad2)
- D7 pad 1: L_ROW3 -> L_ROW1
- D7 pad 2: Net-(D7-Pad2) -> Net-(D6-Pad2)
- D8 pad 1: L_ROW4 -> L_ROW1
- D8 pad 2: Net-(D8-Pad2) -> Net-(D6-Pad2)
- D9 pad 1: L_ROW5 -> L_ROW1
- D9 pad 2: Net-(D9-Pad2) -> Net-(D6-Pad2)
- R10 pad 2: Net-(R13-Pad2) (its old number) -> Net-(R10-Pad2)
- R12 pad 2: Net-(R15-Pad2) (its old number) -> Net-(R12-Pad2)
- R25 pad 2: Net-(R27-Pad2) -> Net-(R25-Pad2)
- R26 pad 2: Net-(R28-Pad2) -> Net-(R26-Pad2)
- R3 pad 2: Net-(R1-Pad2) -> Net-(R3-Pad2)
- R5 pad 2: Net-(R9-Pad2) -> Net-(R5-Pad2)
- R6 pad 2: Net-(R10-Pad2) -> Net-(R6-Pad2)
- R8 pad 2: Net-(R11-Pad2) (its old number) -> Net-(R8-Pad2)
- R9 pad 2: Net-(R12-Pad2) -> Net-(R9-Pad2)
- S1 pad 2: Net-(R1-Pad2) -> Net-(R3-Pad2)
- S10 pad 1: Net-(D10-Pad2) -> Net-(D6-Pad2)
- S10 pad 2: Net-(R12-Pad2) -> Net-(R5-Pad2)
- S11 pad 1: Net-(D11-Pad2) -> Net-(D6-Pad2)
- S11 pad 2: Net-(R12-Pad2) -> Net-(R5-Pad2)
- S12 pad 1: Net-(D12-Pad2) -> Net-(D6-Pad2)
- S12 pad 2: Net-(R12-Pad2) -> Net-(R5-Pad2)
- S13 pad 1: Net-(D13-Pad2) -> Net-(D6-Pad2)
- S13 pad 2: Net-(R12-Pad2) -> Net-(R5-Pad2)
- S14 pad 1: Net-(D14-Pad2) -> Net-(D6-Pad2)
- S14 pad 2: Net-(R12-Pad2) -> Net-(R5-Pad2)
- S15 pad 1: Net-(D15-Pad2) -> Net-(D6-Pad2)
- S15 pad 2: Net-(R11-Pad2) (its old number) -> Net-(R5-Pad2)
- S16 pad 1: Net-(D16-Pad2) -> Net-(D6-Pad2)
- S16 pad 2: Net-(R11-Pad2) (its old number) -> Net-(R5-Pad2)
- S17 pad 1: Net-(D17-Pad2) -> Net-(D6-Pad2)
- S17 pad 2: Net-(R11-Pad2) (its old number) -> Net-(R5-Pad2)
- S18 pad 1: Net-(D18-Pad2) -> Net-(D6-Pad2)
- S18 pad 2: Net-(R11-Pad2) (its old number) -> Net-(R5-Pad2)
- S19 pad 1: Net-(D19-Pad2) -> Net-(D6-Pad2)
- S19 pad 2: Net-(R11-Pad2) (its old number) -> Net-(R5-Pad2)
- S2 pad 1: Net-(D2-Pad2) -> Net-(D6-Pad2)
- S2 pad 2: Net-(R15-Pad2) (its old number) -> Net-(R5-Pad2)
- S20 pad 1: Net-(D20-Pad2) -> Net-(D6-Pad2)
- S20 pad 2: Net-(R10-Pad2) -> Net-(R5-Pad2)
- S21 pad 1: Net-(D21-Pad2) -> Net-(D6-Pad2)
- S21 pad 2: Net-(R10-Pad2) -> Net-(R5-Pad2)
- S22 pad 1: Net-(D22-Pad2) -> Net-(D6-Pad2)
- S22 pad 2: Net-(R10-Pad2) -> Net-(R5-Pad2)
- S23 pad 1: Net-(D23-Pad2) -> Net-(D6-Pad2)
- S23 pad 2: Net-(R10-Pad2) -> Net-(R5-Pad2)
- S24 pad 1: Net-(D24-Pad2) -> Net-(D6-Pad2)
- S24 pad 2: Net-(R10-Pad2) -> Net-(R5-Pad2)
- S26 pad 1: Net-(D26-Pad2) -> Net-(D6-Pad2)
- S26 pad 2: Net-(R9-Pad2) -> Net-(R5-Pad2)
- S3 pad 1: Net-(D3-Pad2) -> Net-(D6-Pad2)
- S3 pad 2: Net-(R15-Pad2) (its old number) -> Net-(R5-Pad2)
- S30 pad 1: Net-(D30-Pad2) (its old number) -> Net-(D6-Pad2)
- S30 pad 2: Net-(R1-Pad2) -> Net-(R5-Pad2)
- S31 pad 1: Net-(D31-Pad2) (its old number) -> Net-(D6-Pad2)
- S31 pad 2: Net-(R1-Pad2) -> Net-(R5-Pad2)
- S4 pad 1: Net-(D25-Pad2) -> Net-(D6-Pad2)
- S4 pad 2: Net-(R9-Pad2) -> Net-(R5-Pad2)
- S5 pad 1: Net-(D5-Pad2) (its old number) -> Net-(D6-Pad2)
- S5 pad 2: Net-(R13-Pad2) (its old number) -> Net-(R5-Pad2)
- S6 pad 2: Net-(R13-Pad2) (its old number) -> Net-(R5-Pad2)
- S62 pad 2: Net-(R27-Pad2) -> Net-(R25-Pad2)
- S63 pad 2: Net-(R27-Pad2) -> Net-(R25-Pad2)
- S64 pad 2: Net-(R28-Pad2) -> Net-(R25-Pad2)
- S65 pad 2: Net-(R28-Pad2) -> Net-(R25-Pad2)
- S66 pad 2: Net-(R27-Pad2) -> Net-(R25-Pad2)
- S67 pad 2: Net-(R28-Pad2) -> Net-(R26-Pad2)
- S7 pad 1: Net-(D7-Pad2) -> Net-(D6-Pad2)
- S7 pad 2: Net-(R13-Pad2) (its old number) -> Net-(R5-Pad2)
- S70 pad 2: Net-(R28-Pad2) -> Net-(R26-Pad2)
- S8 pad 1: Net-(D8-Pad2) -> Net-(D6-Pad2)
- S8 pad 2: Net-(R13-Pad2) (its old number) -> Net-(R5-Pad2)
- S9 pad 1: Net-(D9-Pad2) -> Net-(D6-Pad2)
- S9 pad 2: Net-(R13-Pad2) (its old number) -> Net-(R5-Pad2)
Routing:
- net L_ROW2: track 128.4 -> 0.00 mm
- net L_ROW5: track 124.5 -> 0.00 mm
- net R_ROW2: track 124.5 -> 0.00 mm
- net R_ROW5: track 124.2 -> 0.00 mm
- net R_ROW3: track 115.0 -> 0.00 mm
- net L_ROW4: track 115.0 -> 0.00 mm
- net R_ROW4: track 114.9 -> 0.00 mm
- net L_ROW3: track 114.8 -> 0.00 mm
- net Net-(D6-Pad2): track 3.70 -> 100.9 mm
- net Net-(R27-Pad2): track 87.1 -> 0.00 mm
- net R_ROW1: track 80.7 -> 0.00 mm
- net L_ROW1: track 80.6 -> 0.00 mm
- net Net-(R13-Pad2) (its old number): track 77.3 -> 0.00 mm
- net Net-(R12-Pad2): track 77.2 -> 0.00 mm
- net Net-(R10-Pad2): track 76.1 -> 0.00 mm
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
